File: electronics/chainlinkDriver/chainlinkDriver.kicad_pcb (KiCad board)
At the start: 2 copper layers, 198.1 x 30.5 mm, 66 parts, among them J1 Inputs_B, J10 Sensor C, J11 Sensor D, J12 Motor E, J13 Motor F, J14 Sensor E, J15 Sensor F, J16 Power_B, J17 Outputs_A, J18 Outputs_B, J2 Inputs_A, J3 Motor A, J4 Power_A, J5 Motor B, J6 Motor C, J7 Motor D, J8 Sensor A, J9 Sensor B, U1 74HC595, U10 TPL7407L, U2 TPL7407L, U3 74HC125, U4 74HC165, U5 74HC595, U6 TPL7407L, U7 74HC595, U8 TPL7407L, U9 74HC595

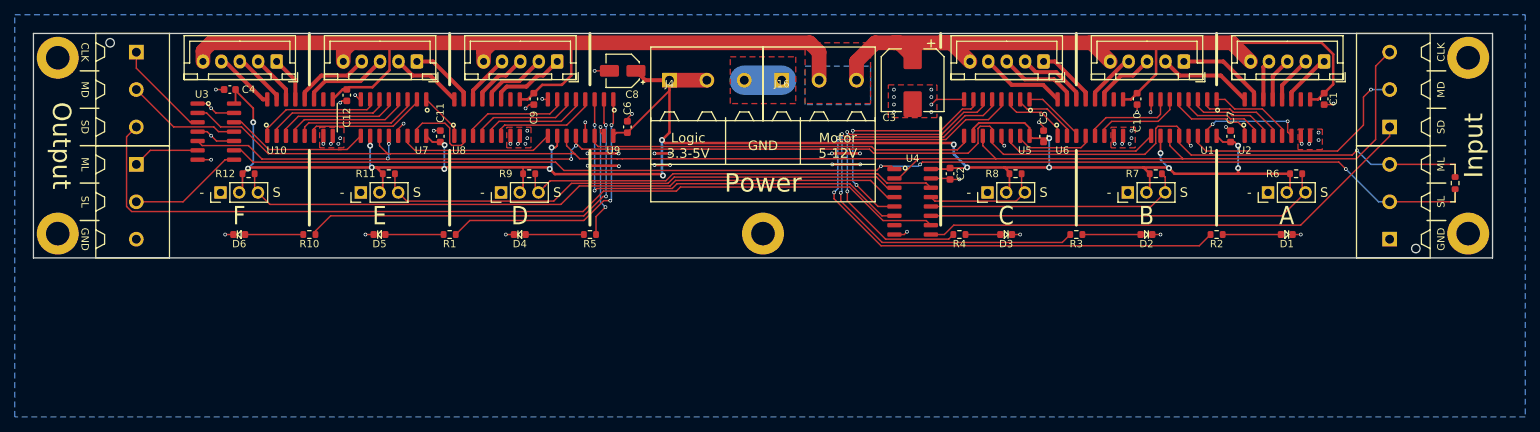
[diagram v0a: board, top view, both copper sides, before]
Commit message: Change screw terminals from 3-pin groups to more common 2-pin groups
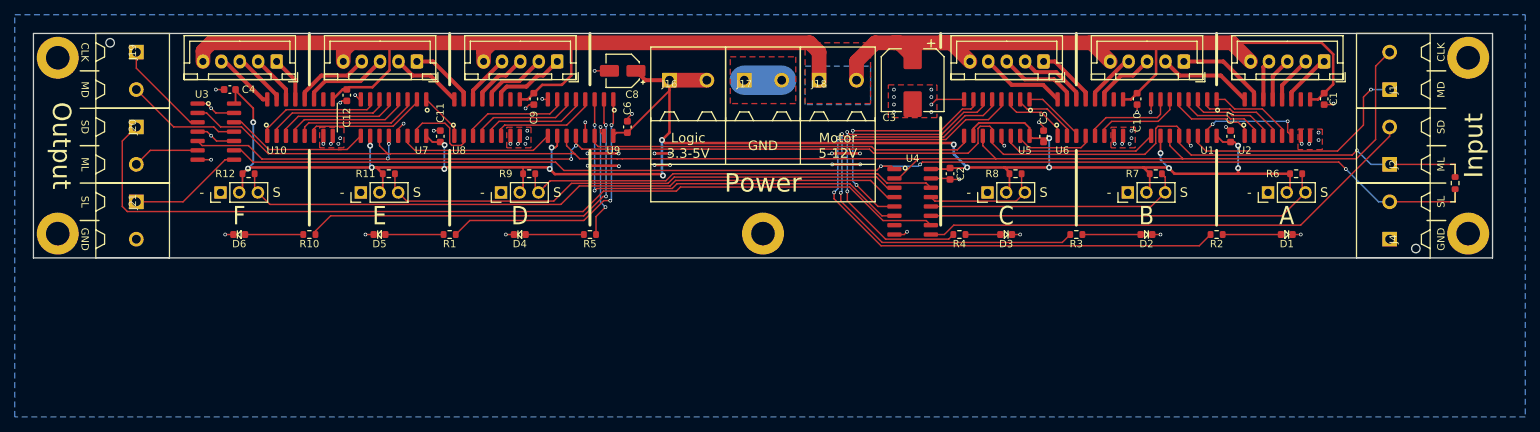
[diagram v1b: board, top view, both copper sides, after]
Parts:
- added J19: Outputs, ScrewTerminals:C8465_WJ500V-5.08-2P, F.Cu at (39.4, 27.9)
- added J20: Outputs, ScrewTerminals:C8465_WJ500V-5.08-2P, F.Cu at (39.4, 38.1)
- added J21: Outputs, ScrewTerminals:C8465_WJ500V-5.08-2P, F.Cu at (39.4, 48.3)
- J1: value Inputs_B -> Inputs; footprint ScrewTerminals:C72334_WJ500V-5.08-3P -> ScrewTerminals:C8465_WJ500V-5.08-2P
- J16: value Power_B -> Power; footprint ScrewTerminals:C72334_WJ500V-5.08-3P -> ScrewTerminals:C8465_WJ500V-5.08-2P
- J17: value Outputs_A -> Power; footprint ScrewTerminals:C72334_WJ500V-5.08-3P -> ScrewTerminals:C8465_WJ500V-5.08-2P
- J18: value Outputs_B -> Power; footprint ScrewTerminals:C72334_WJ500V-5.08-3P -> ScrewTerminals:C8465_WJ500V-5.08-2P
- J2: value Inputs_A -> Inputs; footprint ScrewTerminals:C72334_WJ500V-5.08-3P -> ScrewTerminals:C8465_WJ500V-5.08-2P
- J4: value Power_A -> Inputs; footprint ScrewTerminals:C72334_WJ500V-5.08-3P -> ScrewTerminals:C8465_WJ500V-5.08-2P
- moved J4 100.1 mm to (209.6, 53.3), turned to 90 degrees
- moved J18 93.4 mm to (132.1, 31.8), turned to 0 degrees
- moved J17 82.6 mm to (121.9, 31.8), turned to 0 degrees
- moved J16 15.2 mm to (111.8, 31.8)
- moved J2 10.2 mm to (209.6, 43.2)
- moved J1 5.08 mm to (209.6, 33.0)
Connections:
- J1 pad 1: /SENSOR_OUT -> /MOTOR_IN
- J1 pad 2: /MOTOR_IN -> /CLOCK_IN
- J16 pad 1: GND -> +3V3
- J16 pad 2: +12V -> +3V3
- J17 pad 1: /CLOCK_OUT -> GND
- J17 pad 2: /MOTOR_OUT -> GND
- J18 pad 1: /MOTOR_LATCH_OUT -> +12V
- J18 pad 2: /SENSOR_LATCH_OUT -> +12V
- J2 pad 1: GND -> /MOTOR_LATCH_IN
- J2 pad 2: /SENSOR_LATCH_IN -> /SENSOR_OUT
- J4 pad 1: +3V3 -> GND
- J4 pad 2: +3V3 -> /SENSOR_LATCH_IN
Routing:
- net /SENSOR_IN: track 124.4 -> 125.2 mm
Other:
- board text removed: "ID#"

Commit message: Move screw terminal silkscreen labels, adjust trace
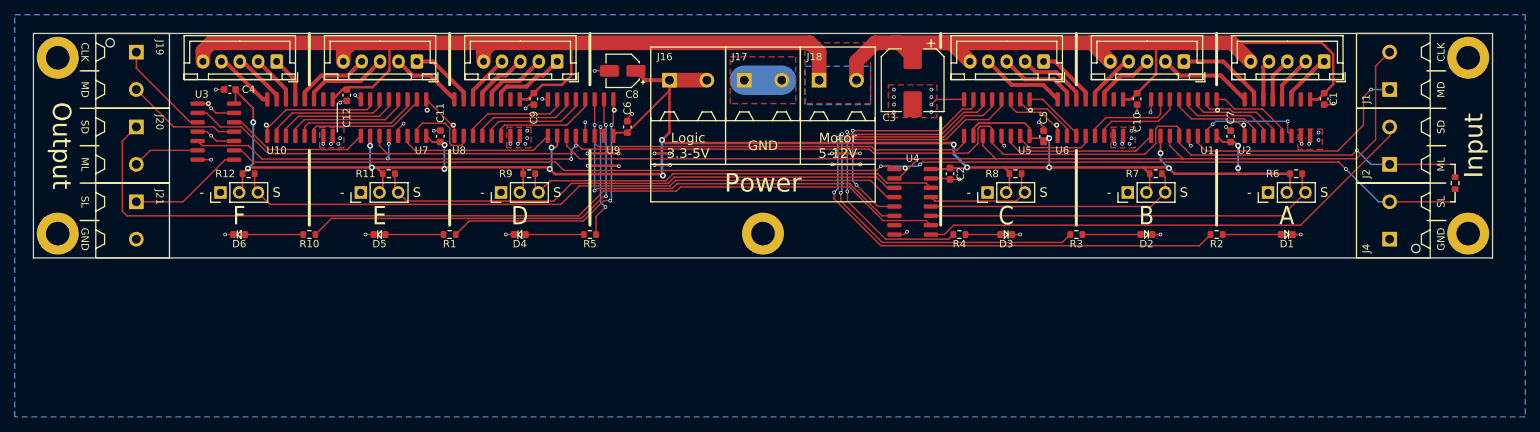
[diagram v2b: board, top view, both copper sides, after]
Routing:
- net /SENSOR_IN: track 125.2 -> 126.0 mm
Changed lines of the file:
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@@
     (thickness 1.6)
     (drawings 79)
-    (tracks 811)
+    (tracks 810)
     (zones 0)
     (modules 69)
@@
     (at 39.37 48.26 270)
     (attr smd)
-    (fp_text reference J21 (at 0 0.5 90) (layer F.SilkS)
+    (fp_text reference J21 (at -0.635 -3.175 270 unlocked) (layer F.SilkS)
       (effects (font (size 1 1) (thickness 0.15)))
     )
@@
     (at 39.37 38.1 270)
     (attr smd)
-    (fp_text reference J20 (at 0 0.5 90) (layer F.SilkS)
+    (fp_text reference J20 (at -0.635 -3.175 270 unlocked) (layer F.SilkS)
       (effects (font (size 1 1) (thickness 0.15)))
     )
@@
     (at 39.37 27.94 270)
     (attr smd)
-    (fp_text reference J19 (at 0 0.5 90) (layer F.SilkS)
+    (fp_text reference J19 (at -0.635 -3.175 270 unlocked) (layer F.SilkS)
       (effects (font (size 1 1) (thickness 0.15)))
     )
@@
     (at 132.08 31.75)
     (attr smd)
-    (fp_text reference J18 (at 0 0.5) (layer F.SilkS)
+    (fp_text reference J18 (at -0.635 -3.175) (layer F.SilkS)
       (effects (font (size 1 1) (thickness 0.15)))
     )
@@
     (at 121.92 31.75)
     (attr smd)
-    (fp_text reference J17 (at 0 0.5) (layer F.SilkS)
+    (fp_text reference J17 (at -0.635 -3.175) (layer F.SilkS)
       (effects (font (size 1 1) (thickness 0.15)))
     )
@@
     (at 111.76 31.75)
     (attr smd)
-    (fp_text reference J16 (at 0 0.5) (layer F.SilkS)
+    (fp_text reference J16 (at -0.635 -3.175) (layer F.SilkS)
       (effects (font (size 1 1) (thickness 0.15)))
     )
@@
     (at 209.55 53.34 90)
     (attr smd)
-    (fp_text reference J4 (at 0 0.5 90) (layer F.SilkS)
+    (fp_text reference J4 (at -1.27 -3.175 90) (layer F.SilkS)
       (effects (font (size 1 1) (thickness 0.15)))
     )
@@
     (at 209.55 43.18 90)
     (attr smd)
-    (fp_text reference J2 (at 0 0.5 90) (layer F.SilkS)
+    (fp_text reference J2 (at -1.27 -3.175 90) (layer F.SilkS)
       (effects (font (size 1 1) (thickness 0.15)))
     )
@@
     (at 209.55 33.02 90)
     (attr smd)
-    (fp_text reference J1 (at 0 0.5 90) (layer F.SilkS)
+    (fp_text reference J1 (at -1.27 -3.175 90) (layer F.SilkS)
       (effects (font (size 1 1) (thickness 0.15)))
     )
@@
   (segment (start 104.14 37.592) (end 103.886 37.846) (width 0.2) (layer F.Cu) (net 69))
   (segment (start 103.886 37.846) (end 103.886 47.94124) (width 0.2) (layer B.Cu) (net 69))
-  (segment (start 102.83557 48.10062) (end 103.72662 48.10062) (width 0.2) (layer F.Cu) (net 69))
   (segment (start 103.886 47.94124) (end 103.72662 48.10062) (width 0.2) (layer B.Cu) (net 69))
-  (segment (start 100.13619 50.8) (end 102.83557 48.10062) (width 0.2) (layer F.Cu) (net 69))
-  (segment (start 84.645 50.8) (end 100.13619 50.8) (width 0.2) (layer F.Cu) (net 69))
-  (segment (start 82.74 52.705) (end 84.645 50.8) (width 0.2) (layer F.Cu) (net 69))
   (via (at 103.72662 48.10062) (size 0.5) (drill 0.3) (layers F.Cu B.Cu) (net 69))
+  (segment (start 102.83557 48.10062) (end 103.72662 48.10062) (width 0.2) (layer F.Cu) (net 69))
+  (segment (start 84.57998 50.86502) (end 100.07117 50.86502) (width 0.2) (layer F.Cu) (net 69))
+  (segment (start 82.74 52.705) (end 84.57998 50.86502) (width 0.2) (layer F.Cu) (net 69))
+  (segment (start 100.07117 50.86502) (end 102.83557 48.10062) (width 0.2) (layer F.Cu) (net 69))
   (via (at 103.152339 47.530555) (size 0.5) (drill 0.3) (layers F.Cu B.Cu) (net 70))
-  (segment (start 63.69 52.705) (end 63.69 52.23) (width 0.2) (layer F.Cu) (net 70))
-  (segment (start 63.69 52.23) (end 65.755 50.165) (width 0.2) (layer F.Cu) (net 70))
-  (segment (start 65.755 50.165) (end 100.134779 50.165) (width 0.2) (layer F.Cu) (net 70))
-  (segment (start 100.134779 50.165) (end 102.769224 47.530555) (width 0.2) (layer F.Cu) (net 70))
-  (segment (start 102.769224 47.530555) (end 103.152339 47.530555) (width 0.2) (layer F.Cu) (net 70))
   (via (at 103.124 37.846) (size 0.5) (drill 0.3) (layers F.Cu B.Cu) (net 70))
   (segment (start 102.87 34.355) (end 102.87 37.592) (width 0.2) (layer F.Cu) (net 70))
@@
   (segment (start 103.152339 47.530555) (end 103.152339 37.874339) (width 0.2) (layer B.Cu) (net 70))
   (segment (start 103.152339 37.874339) (end 103.124 37.846) (width 0.2) (layer B.Cu) (net 70))
+  (segment (start 102.798786 47.530555) (end 103.152339 47.530555) (width 0.2) (layer F.Cu) (net 70))
+  (segment (start 99.81433 50.515011) (end 102.798786 47.530555) (width 0.2) (layer F.Cu) (net 70))
+  (segment (start 65.879989 50.515011) (end 99.81433 50.515011) (width 0.2) (layer F.Cu) (net 70))
+  (segment (start 63.69 52.705) (end 65.879989 50.515011) (width 0.2) (layer F.Cu) (net 70))
   (segment (start 95.25 39.305) (end 93.275042 41.279958) (width 0.2) (layer F.Cu) (net 71))
   (segment (start 93.275042 41.279958) (end 77.199958 41.279958) (width 0.2) (layer F.Cu) (net 71))
@@
   (segment (start 149.087522 52.705) (end 150.357522 51.435) (width 0.2) (layer F.Cu) (net 80))
   (segment (start 147.255 52.705) (end 149.087522 52.705) (width 0.2) (layer F.Cu) (net 80) (status 10))
+  (segment (start 146.62999 50.80999) (end 147.255 51.435) (width 0.2) (layer F.Cu) (net 81))
+  (segment (start 136.207335 46.256329) (end 140.760996 50.80999) (width 0.2) (layer F.Cu) (net 81))
+  (segment (start 112.706446 46.805554) (end 113.255671 46.256329) (width 0.2) (layer F.Cu) (net 81))
   (segment (start 113.255671 46.256329) (end 136.207335 46.256329) (width 0.2) (layer F.Cu) (net 81))
   (segment (start 102.804338 46.805554) (end 112.706446 46.805554) (width 0.2) (layer F.Cu) (net 81))
+  (segment (start 38.1 50.165) (end 99.444892 50.165) (width 0.2) (layer F.Cu) (net 81))
   (segment (start 140.760996 50.80999) (end 146.62999 50.80999) (width 0.2) (layer F.Cu) (net 81))
-  (segment (start 38.155001 49.585001) (end 100.024891 49.585001) (width 0.2) (layer F.Cu) (net 81))
-  (segment (start 37.465 48.895) (end 38.155001 49.585001) (width 0.2) (layer F.Cu) (net 81))
-  (segment (start 146.62999 50.80999) (end 147.255 51.435) (width 0.2) (layer F.Cu) (net 81))
-  (segment (start 112.706446 46.805554) (end 113.255671 46.256329) (width 0.2) (layer F.Cu) (net 81))
-  (segment (start 100.024891 49.585001) (end 102.804338 46.805554) (width 0.2) (layer F.Cu) (net 81))
-  (segment (start 37.465 40.005) (end 37.465 48.895) (width 0.2) (layer F.Cu) (net 81))
-  (segment (start 136.207335 46.256329) (end 140.760996 50.80999) (width 0.2) (layer F.Cu) (net 81))
+  (segment (start 99.444892 50.165) (end 102.804338 46.805554) (width 0.2) (layer F.Cu) (net 81))
+  (segment (start 37.465 49.53) (end 38.1 50.165) (width 0.2) (layer F.Cu) (net 81))
+  (segment (start 37.465 40.005) (end 37.465 49.53) (width 0.2) (layer F.Cu) (net 81))
   (segment (start 39.37 38.1) (end 37.465 40.005) (width 0.2) (layer F.Cu) (net 81))
   (segment (start 218.44 44.895) (end 218.44 43.18) (width 0.2) (layer F.Cu) (net 82) (status 10))

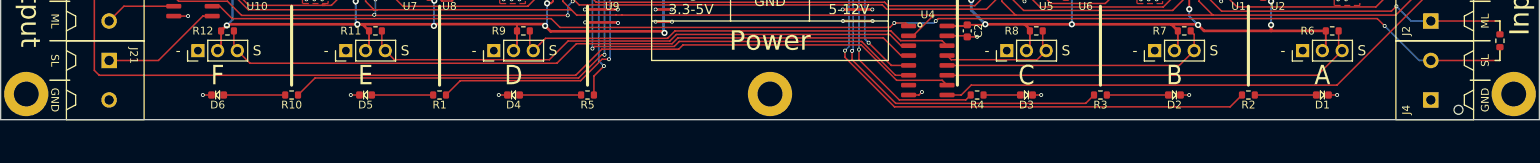
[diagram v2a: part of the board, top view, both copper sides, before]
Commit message: chainlinkDriver: add sensor input pulldown, change shield terminal label from GND to SHD
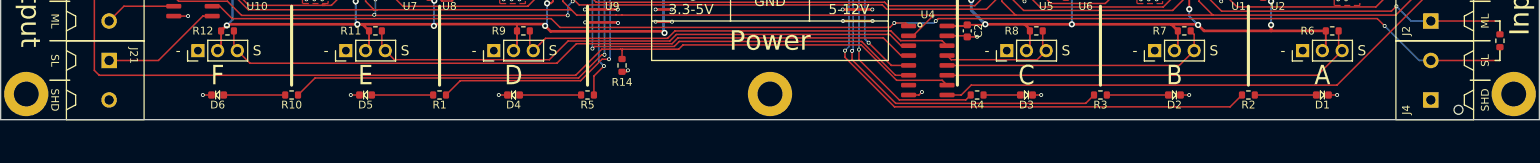
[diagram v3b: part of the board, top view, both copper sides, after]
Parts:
- added R14: 47k, Resistor_SMD:R_0603_1608Metric, F.Cu at (105.4, 48.9)
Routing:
- net /SENSOR_IN: track 126.0 -> 127.3 mm
- net GND: track 78.3 -> 79.2 mm, vias 66 -> 67
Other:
- board text added: "SHD"

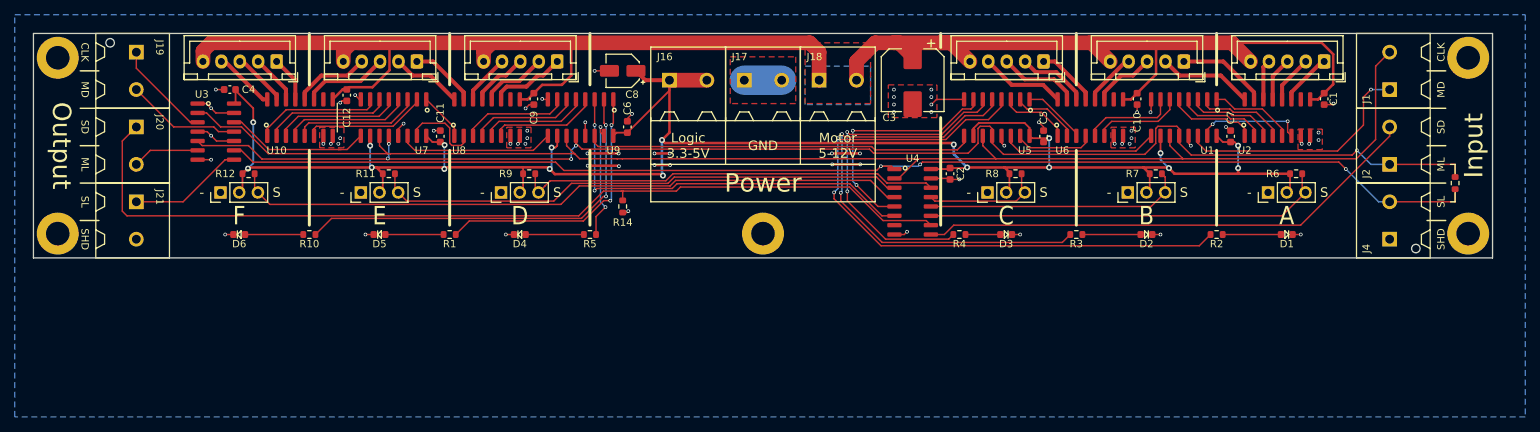
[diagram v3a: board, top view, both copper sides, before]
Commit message: Combine latch signals, replace screw terminals with 2x4 IDC connectors
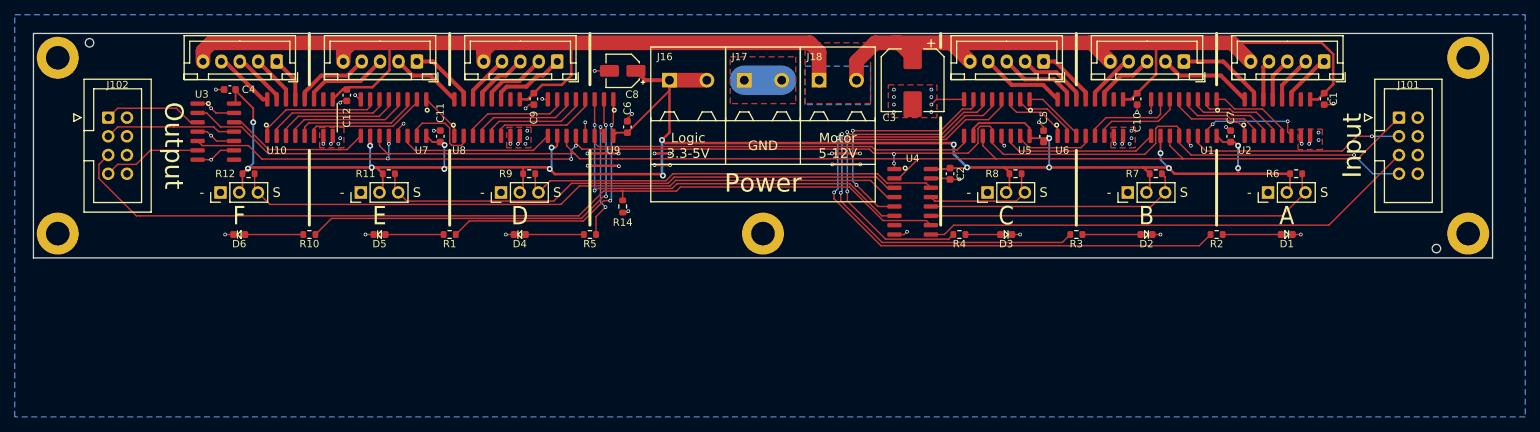
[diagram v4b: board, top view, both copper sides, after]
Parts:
- removed J1, J2, J4: Inputs, ScrewTerminals:C8465_WJ500V-5.08-2P
- removed J19, J20, J21: Outputs, ScrewTerminals:C8465_WJ500V-5.08-2P
- removed R13: 0R, Resistor_SMD:R_0603_1608Metric
- added J101: Input, Connector_IDC:IDC-Header_2x04_P2.54mm_Vertical, F.Cu at (210.8, 36.8)
- added J102: Output, Connector_IDC:IDC-Header_2x04_P2.54mm_Vertical, F.Cu at (35.6, 36.8)
- moved H7 2.79 mm to (215.9, 54.6)
- moved H6 2.79 mm to (33.0, 26.7)
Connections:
- U1 pad 12: /MOTOR_LATCH_IN -> /LATCH_IN
- U3 pad 5: /MOTOR_LATCH_IN -> /LATCH_IN
- U3 pad 6: /MOTOR_LATCH_OUT -> /LATCH_OUT
- U3 pad 8: /SENSOR_LATCH_OUT -> (no net)
- U3 pad 9: /SENSOR_LATCH_IN -> GND
- U4 pad 1: /SENSOR_LATCH_IN -> /LATCH_IN
- U5 pad 12: /MOTOR_LATCH_IN -> /LATCH_IN
- U7 pad 12: /MOTOR_LATCH_IN -> /LATCH_IN
- U9 pad 12: /MOTOR_LATCH_IN -> /LATCH_IN
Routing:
- net /MOTOR_LATCH_IN: track 193.0 -> 0.00 mm, vias 5 -> 0
- net /LATCH_IN: track 0.00 -> 186.0 mm, vias 0 -> 7
- net /SENSOR_LATCH_IN: track 173.4 -> 0.00 mm, vias 3 -> 0
- net /SENSOR_LATCH_OUT: track 15.6 -> 0.00 mm
- net /LATCH_OUT: track 0.00 -> 13.4 mm
- net /MOTOR_LATCH_OUT: track 9.11 -> 0.00 mm
- net /CLOCK_IN: track 196.4 -> 188.1 mm
- net GND: track 79.2 -> 82.8 mm
- net /MOTOR_IN: track 33.1 -> 29.6 mm
- net /SENSOR_IN: track 127.3 -> 123.8 mm
- net /MOTOR_OUT: track 15.6 -> 17.9 mm
- net /SENSOR_OUT: track 69.1 -> 68.0 mm
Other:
- board text removed: "CLK"
- board text removed: "MD"
- board text removed: "ML"
- board text removed: "SD"
- board text removed: "SHD"
- board text removed: "SL"
